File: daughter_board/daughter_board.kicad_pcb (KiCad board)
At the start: 2 copper layers, 99.1 x 48.3 mm, 7 parts, among them J1 AudioJack4, SW1 SW_Push, SW2 Rotary_Encoder

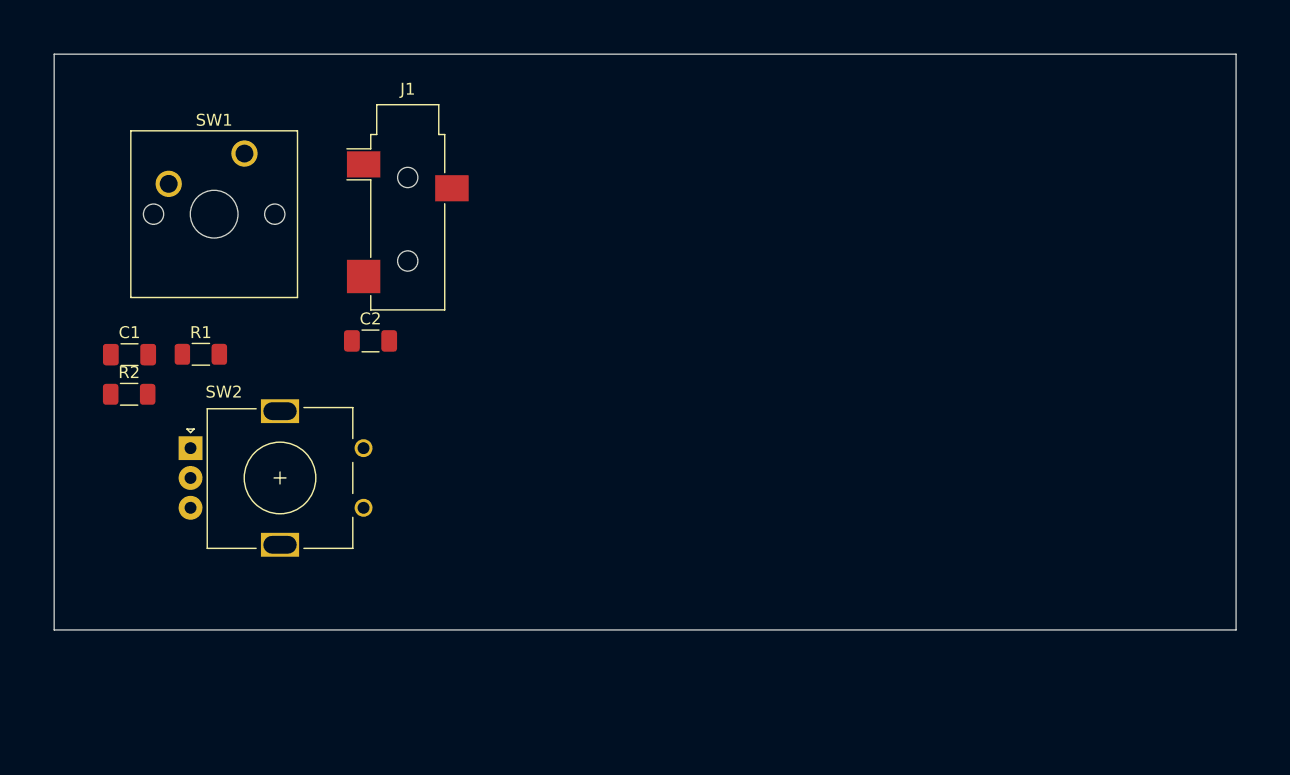
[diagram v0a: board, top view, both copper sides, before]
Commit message: modified connector location to avoid clerance issues
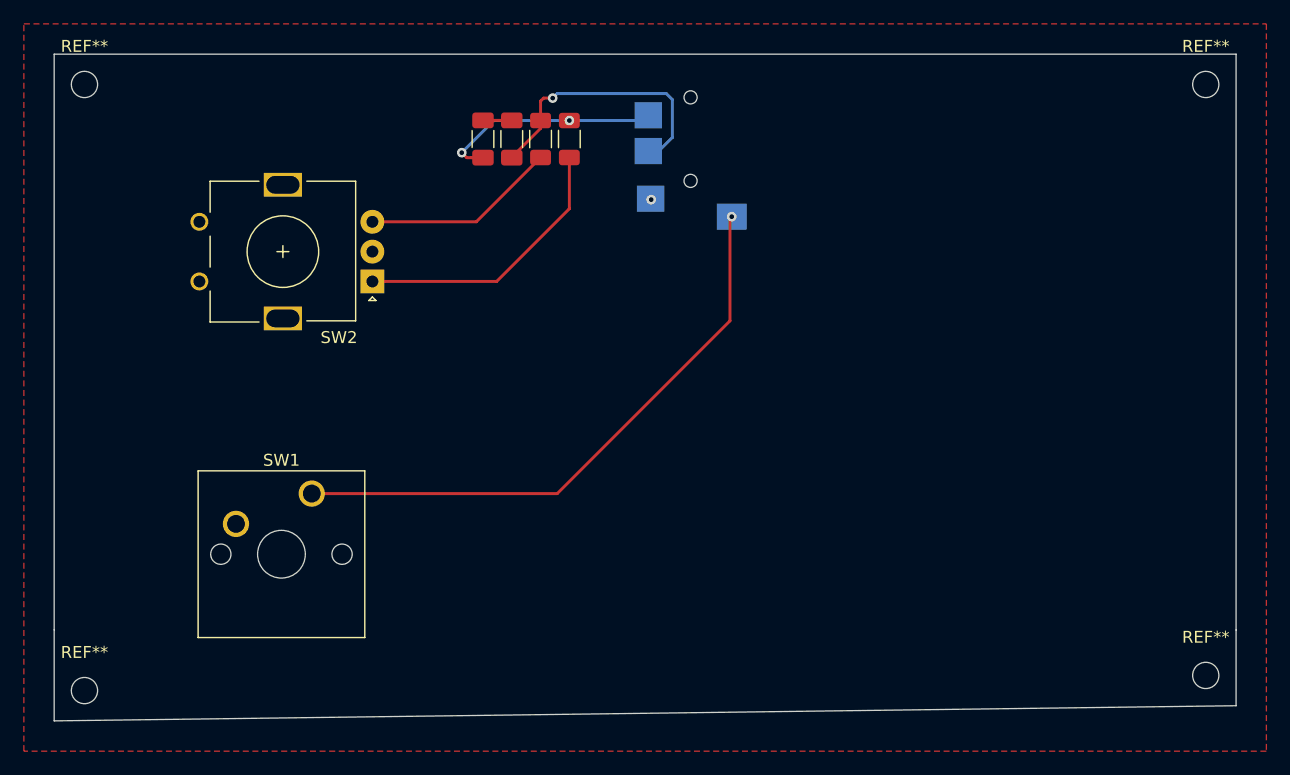
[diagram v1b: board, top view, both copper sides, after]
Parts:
- added REF**: MountingHole_2.2mm_M2, MountingHole:MountingHole_2.2mm_M2, F.Cu at (127.0, 119.4)
- added REF**: MountingHole_2.2mm_M2, MountingHole:MountingHole_2.2mm_M2, F.Cu at (221.0, 118.1)
- added REF**: MountingHole_2.2mm_M2, MountingHole:MountingHole_2.2mm_M2, F.Cu at (221.0, 68.6)
- added REF**: MountingHole_2.2mm_M2, MountingHole:MountingHole_2.2mm_M2, F.Cu at (127.0, 68.6)
- J1: value AudioJack4 -> SJ2-3574A-SMT-TR; footprint Connector_Audio:Jack_3.5mm_CUI_SJ-3523-SMT_Horizontal -> TRRS_jack:CUI_SJ2-3574A-SMT-TR; moved to B.Cu
- R1, R2: value R -> 10K
- moved R2 40.6 mm to (165.2, 73.2), turned to 90 degrees
- moved R1 35.8 mm to (167.6, 73.2), turned to 90 degrees
- moved C1 34.7 mm to (160.4, 73.2), turned to 90 degrees
- moved SW1 29.1 mm to (146.1, 102.9)
- moved J1 24.3 mm to (177.8, 73.7), turned to 270 degrees
- moved SW2 20.7 mm to (151.1, 85.1), turned to 180 degrees
- moved C2 20.7 mm to (162.8, 73.2), turned to 90 degrees
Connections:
- SW1 pad 1: Net-(J1-PadS) -> Net-(J1-Pad1)
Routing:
- net Net-(J1-Pad1): track 0.00 -> 49.8 mm, vias 0 -> 1
- net Net-(R1-Pad1): track 0.00 -> 25.1 mm
- net OUT_B: track 0.00 -> 22.9 mm, vias 0 -> 1
- net OUT_A: track 0.00 -> 19.9 mm, vias 0 -> 2
- net Net-(R2-Pad1): track 0.00 -> 17.2 mm
- net GND: track 0.00 -> 3.09 mm, vias 0 -> 1
- added copper zone on F.Cu, net GND
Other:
- board size 99.1 x 48.3 mm -> 99.1 x 55.9 mm

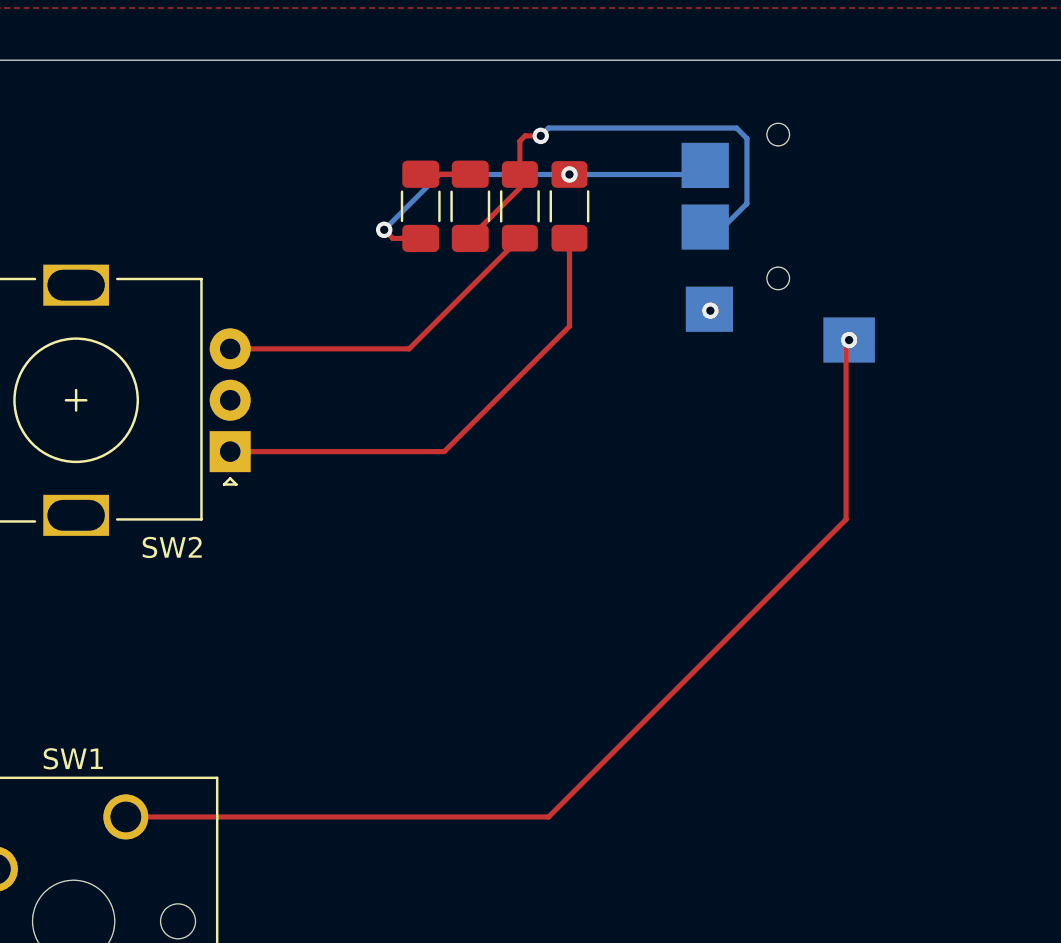
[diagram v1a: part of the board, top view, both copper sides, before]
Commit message: updated trrs jack, old one was out of stock :(
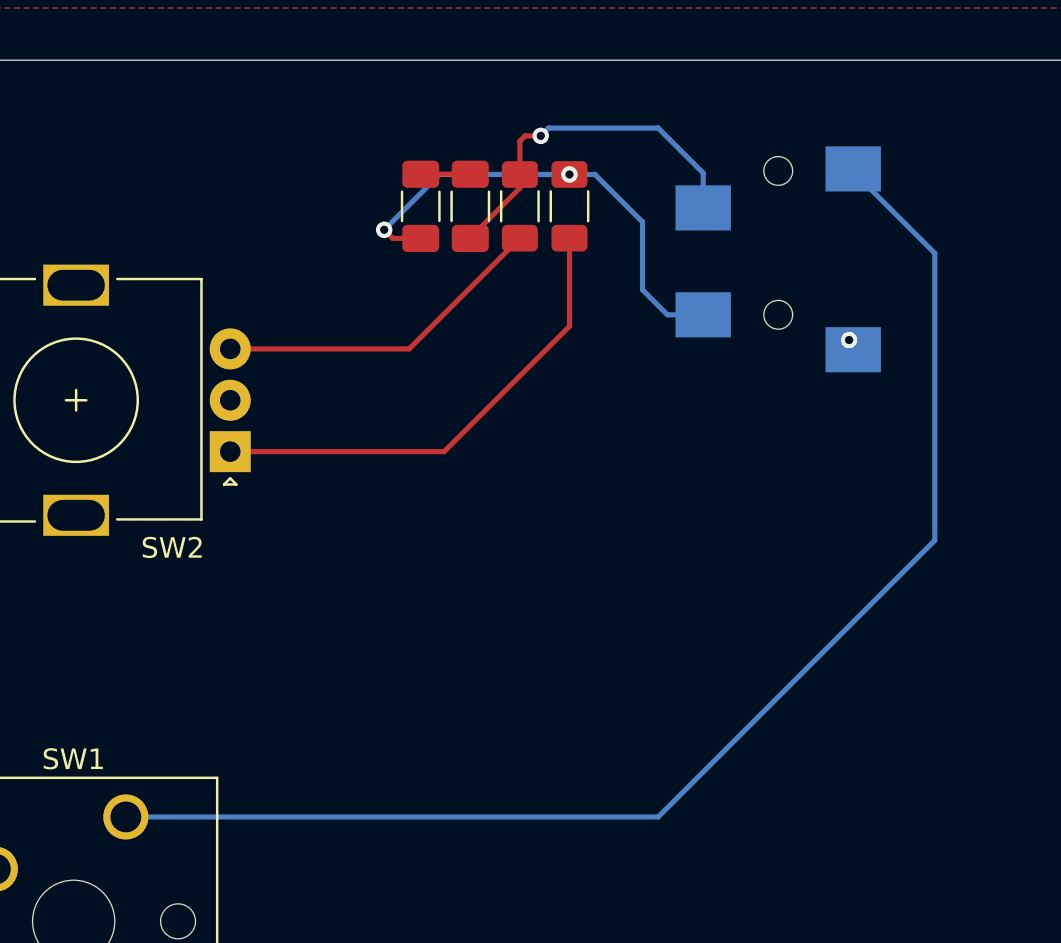
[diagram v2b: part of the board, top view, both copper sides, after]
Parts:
- J1: footprint TRRS_jack:CUI_SJ2-3574A-SMT-TR -> TRRS_jack:CUI_SJ2-35043A-SMT-TR
- moved J1 1.27 mm to (177.8, 74.9)
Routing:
- net Net-(J1-Pad1): track 49.8 -> 64.7 mm, vias 1 -> 0
- net OUT_B: track 22.9 -> 18.4 mm
- net OUT_A: track 19.9 -> 24.3 mm

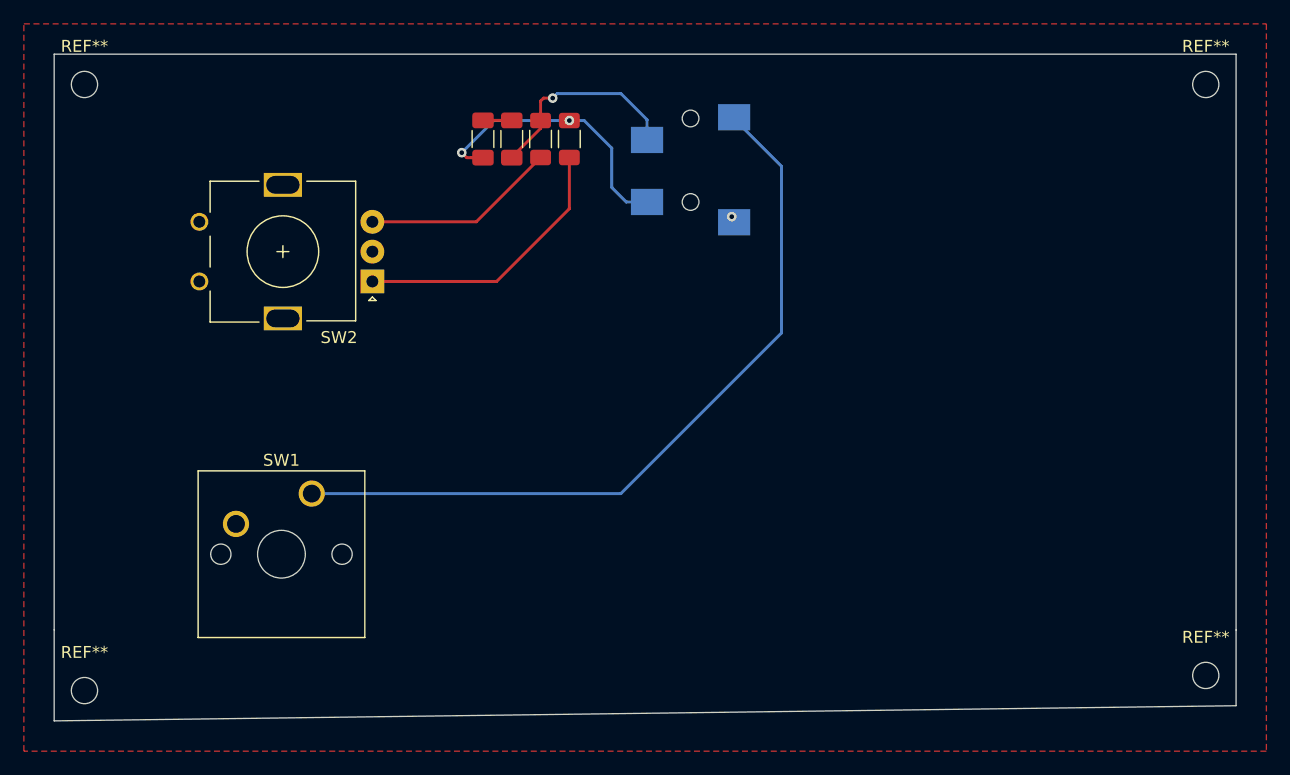
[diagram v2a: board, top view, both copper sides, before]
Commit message: updated TRRS jack bc previous one was wrong one
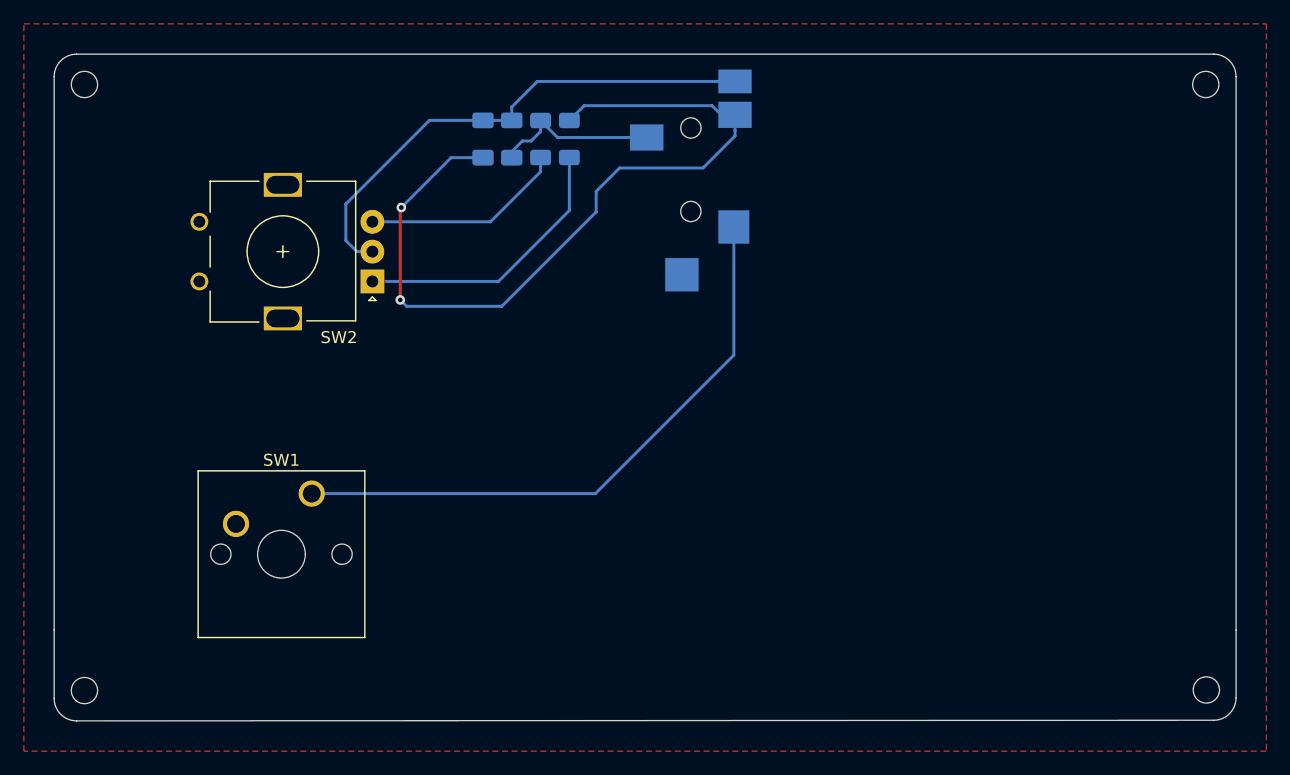
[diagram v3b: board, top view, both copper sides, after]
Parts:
- C1, C2, R1, R2: moved to B.Cu
- J1: value SJ2-3574A-SMT-TR -> SJ-43515TS-SMT; footprint TRRS_jack:CUI_SJ2-35043A-SMT-TR -> TRRS_jack:CUI_SJ-43515TS-SMT
- moved REF** 1.22 mm to (221.0, 119.3)
- moved J1 0.55 mm to (177.8, 75.5)
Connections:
- J1 pad 1: Net-(J1-Pad1) -> GND
- J1 pad 2: GND -> Net-(J1-Pad2)
- SW1 pad 1: Net-(J1-Pad1) -> Net-(J1-Pad2)
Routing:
- net Net-(J1-Pad1): track 64.7 -> 0.00 mm
- net Net-(J1-Pad2): track 0.00 -> 50.9 mm
- net OUT_A: track 24.3 -> 68.3 mm
- net GND: track 3.30 -> 43.9 mm, vias 1 -> 0
- net OUT_B: track 18.4 -> 14.0 mm, vias 1 -> 0
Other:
- outline, holes or cut-outs redrawn
